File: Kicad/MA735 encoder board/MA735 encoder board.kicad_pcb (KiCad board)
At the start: 2 copper layers, 10.4 x 9.5 mm, 5 parts, among them J2 JST SH SM06B, U1 MA735GGU-Z

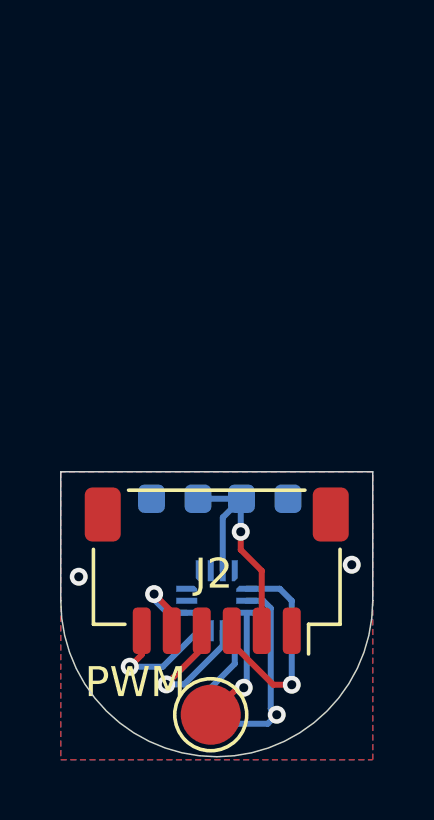
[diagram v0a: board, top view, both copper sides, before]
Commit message: Start redesign of encoder board for flex circuit
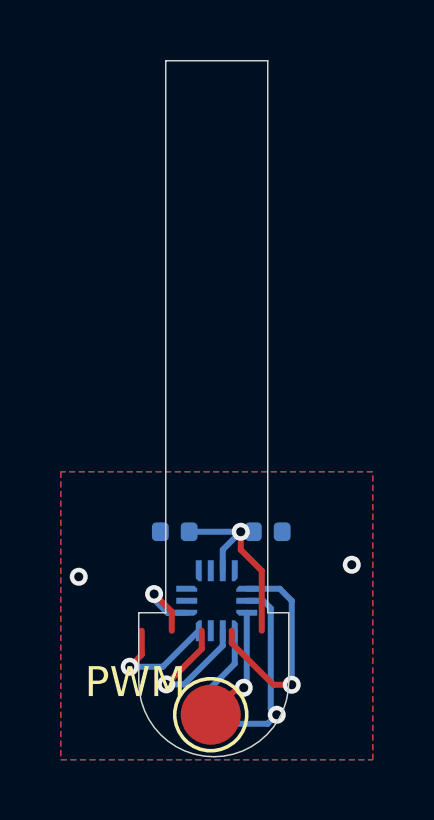
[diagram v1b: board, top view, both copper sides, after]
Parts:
- removed J2: JST SH SM06B, Connector_JST:JST_SH_SM06B-SRSS-TB_1x06-1MP_P1.00mm_Horizontal
- C1, C2: footprint Capacitor_SMD:C_0603_1608Metric -> Capacitor_SMD:C_0402_1005Metric
- moved C1 1.10 mm to (154.1, 84.5)
- moved C2 1.10 mm to (151.0, 84.5)
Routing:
- net +3V3: track 8.77 -> 7.28 mm
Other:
- board size 10.4 x 9.5 mm -> 5 x 23.2 mm

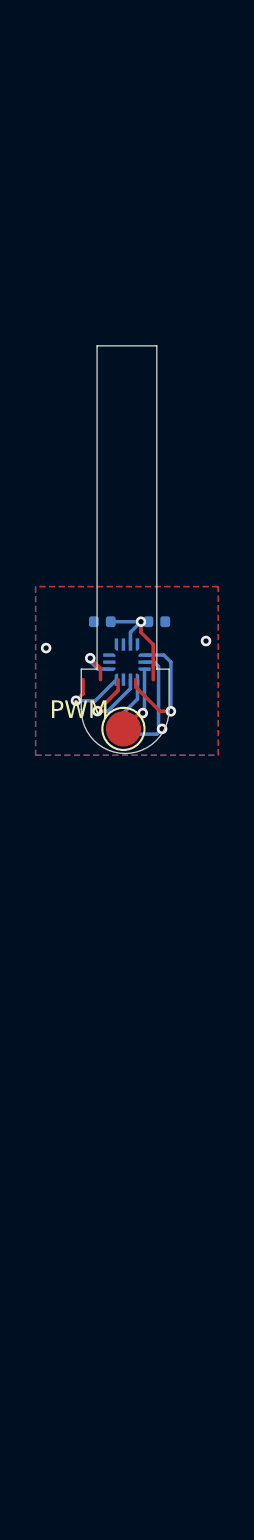
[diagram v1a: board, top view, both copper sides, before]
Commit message: Partial layout complete
I currently have the board sized at 4.5mm with a really long cable. This is probably WAY to small, I can barely fit the 0402 capacitors.
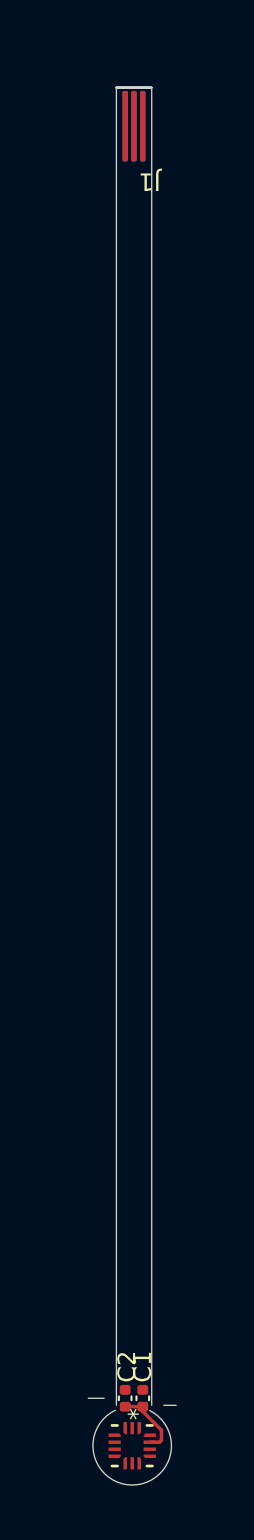
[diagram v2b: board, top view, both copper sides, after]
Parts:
- removed TP1: TestPoint, TestPoint:TestPoint_Pad_D2.0mm
- added J1: FPC top, custom_testpoints:3pin_fpc, F.Cu at (152.8, 56.3)
- added J2: FPC bottom, custom_testpoints:3pin_fpc, B.Cu at (152.8, 56.3)
- C1, C2, U1: moved to F.Cu
- moved U1 44.6 mm to (152.7, 131.4), turned to -90 degrees
- moved C2 44.2 mm to (152.3, 128.7), turned to 90 degrees
- moved C1 44.2 mm to (153.3, 128.7), turned to 90 degrees
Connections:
- U1 pad 3: /PWM -> unconnected-(U1-PWM-Pad3)
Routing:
- net GND: track 10.3 -> 0.00 mm, vias 3 -> 0
- net /SCK: track 7.45 -> 0.00 mm, vias 1 -> 0
- net /MISO: track 5.19 -> 0.00 mm, vias 1 -> 0
- net /CS: track 4.16 -> 0.00 mm, vias 1 -> 0
- net /PWM: track 4.01 -> 0.00 mm, vias 1 -> 0
- net +3V3: track 7.28 -> 4.06 mm, vias 1 -> 0
- net /MOSI: track 2.93 -> 0.00 mm, vias 1 -> 0
- removed copper zone on B.Cu, net GND
- removed copper zone on F.Cu, net GND
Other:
- board size 5 x 23.2 mm -> 5 x 79.5 mm
- board text removed: "PWM"

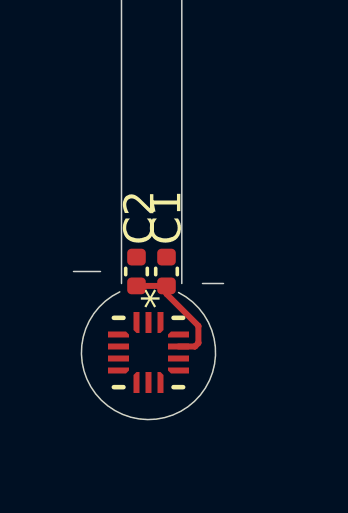
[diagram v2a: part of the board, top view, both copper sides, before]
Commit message: Mostly completed routing
I have reached the minimum obtainable space, 5.6mm diameter. I don't think is not worth it to try shrinking it smaller
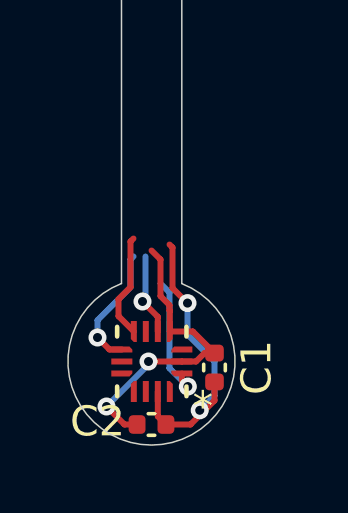
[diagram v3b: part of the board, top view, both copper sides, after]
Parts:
- moved C2 5.12 mm to (152.8, 133.8), turned to 180 degrees
- moved C1 3.58 mm to (154.9, 131.9)
- moved U1 0.32 mm to (152.8, 131.7), turned to 180 degrees
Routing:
- net GND: track 0.00 -> 10.4 mm, vias 0 -> 2
- net +3V3: track 4.06 -> 10.1 mm, vias 0 -> 2
- net /SCK: track 0.00 -> 4.33 mm, vias 0 -> 1
- net /MOSI: track 0.00 -> 4.17 mm, vias 0 -> 1
- net /CS: track 0.00 -> 3.52 mm
- net /MISO: track 0.00 -> 2.75 mm, vias 0 -> 1
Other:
- board size 5 x 79.5 mm -> 5.6 x 80.4 mm

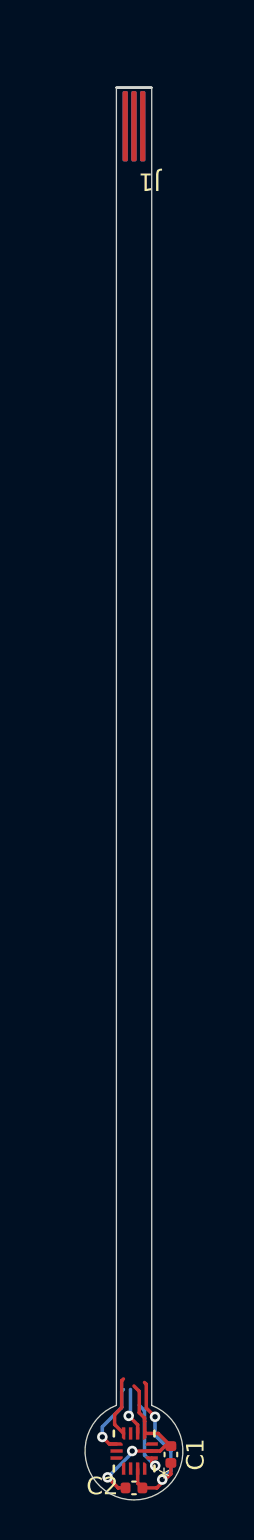
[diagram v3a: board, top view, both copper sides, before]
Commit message: Started work on FPC edge connector
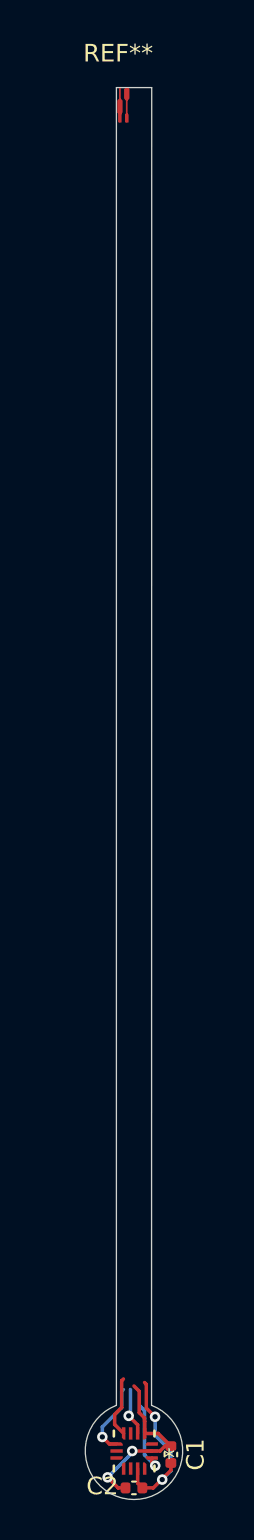
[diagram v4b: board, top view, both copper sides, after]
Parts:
- removed J1: FPC top, custom_testpoints:3pin_fpc
- removed J2: FPC bottom, custom_testpoints:3pin_fpc
- added REF**: 7pin_fpc_contact_0.3mmptich, custom_testpoints:7pin_fpc_contact_0.3mmptich, F.Cu at (152.8, 55.3)
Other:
- board size 5.6 x 80.4 mm -> 5.5 x 80.4 mm
- board text added: "Minimum solder mask is 0.5mm. I have to remove more around the edge connector and the encode"

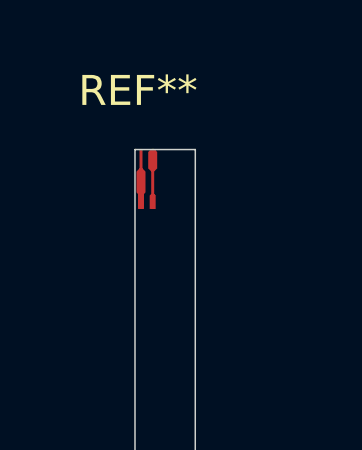
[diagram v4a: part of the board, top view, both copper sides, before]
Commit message: Finished 7pin fpc contacts
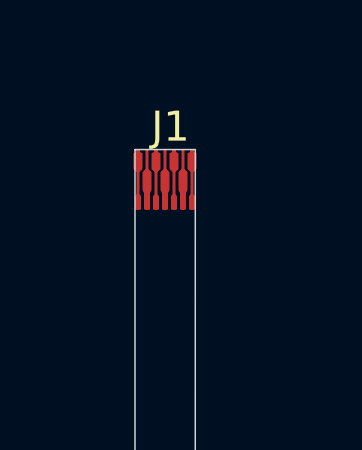
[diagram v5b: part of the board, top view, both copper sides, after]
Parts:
- removed REF**: 7pin_fpc_contact_0.3mmptich, custom_testpoints:7pin_fpc_contact_0.3mmptich
- added J1: FPC contacts 0.3mm, custom_testpoints:7pin_fpc_contact_0.3mmptich, F.Cu at (152.8, 55.2)
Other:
- board text added: "Fits connector: AYF330735 from panasonic"
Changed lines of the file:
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@@
 	(footprint "custom_testpoints:7pin_fpc_contact_0.3mmptich"
 		(layer "F.Cu")
-		(at 152.8 55.3)
-		(property "Reference" "REF**"
-			(at -0.9 -3.15 0)
+		(at 152.8 55.2)
+		(property "Reference" "J1"
+			(at 0.18 -1.86 0)
 			(unlocked yes)
 			(layer "F.SilkS")
@@
 			)
 		)
-		(property "Value" "7pin_fpc_contact_0.3mmptich"
-			(at 4.74 -0.37 0)
+		(property "Value" "FPC contacts 0.3mm"
+			(at 1 0.8 0)
 			(unlocked yes)
 			(layer "F.Fab")
@@
 		)
 		(property "Footprint" "custom_testpoints:7pin_fpc_contact_0.3mmptich"
-			(at 0 0 0)
+			(at -0.1 0.12 0)
 			(unlocked yes)
 			(layer "F.Fab")
@@
 		)
 		(property "Datasheet" ""
-			(at 0 0 0)
+			(at -0.1 0.12 0)
 			(unlocked yes)
 			(layer "F.Fab")
@@
 			)
 		)
-		(property "Description" ""
-			(at 0 0 0)
+		(property "Description" "Generic connector, single row, 01x07, script generated"
+			(at -0.1 0.12 0)
 			(unlocked yes)
 			(layer "F.Fab")
@@
 			)
 		)
+		(property ki_fp_filters "Connector*:*_1x??_*")
+		(sheetname "Root")
+		(sheetfile "MA735 encoder board.kicad_sch")
 		(attr smd)
+		(fp_rect
+			(start -1.2 -1.1)
+			(end 1.2 1.9)
+			(stroke
+				(width 0.05)
+				(type default)
+			)
+			(fill none)
+			(layer "Dwgs.User")
+		)
+		(fp_text user "Stiffener box"
+			(at -2.65 2.54 0)
+			(unlocked yes)
+			(layer "Dwgs.User" knockout)
+			(effects
+				(font
+					(size 0.5 0.5)
+					(thickness 0.1)
+					(bold yes)
+				)
+				(justify left bottom)
+			)
+		)
 		(fp_text user "${REFERENCE}"
-			(at 6.41 -2.22 0)
+			(at 0.33 -0.35 0)
 			(unlocked yes)
 			(layer "F.Fab")
@@
 		)
 		(pad "1" connect custom
-			(at -0.8 -0.22)
-			(size 0.1 2)
-			(layers "F.Cu" "F.Mask")
-			(options
-				(clearance outline)
-				(anchor rect)
-			)
-			(primitives
+			(at -0.9 -0.1)
+			(size 0.1 2)
+			(layers "F.Cu" "F.Mask")
+			(net 3 "/MOSI")
+			(pinfunction "Pin_1")
+			(pintype "passive")
+			(options
+				(clearance outline)
+				(anchor rect)
+			)
+			(primitives
+				(gr_poly
+					(pts
+						(xy -0.1 0.55) (xy -0.05 0.5) (xy 0.05 0.5) (xy 0.1 0.55) (xy 0.1 1) (xy -0.1 1)
+					)
+					(width 0)
+					(fill yes)
+				)
+				(gr_poly
+					(pts
+						(xy -0.15 -0.88) (xy -0.12 -0.89) (xy -0.08 -0.91) (xy -0.06 -0.94) (xy -0.05 -0.97) (xy -0.05 -1)
+						(xy 0.05 -1) (xy 0.05 -0.97) (xy 0.06 -0.94) (xy 0.08 -0.91) (xy 0.12 -0.89) (xy 0.15 -0.88) (xy 0.15 -0.35)
+						(xy 0.05 -0.25) (xy -0.05 -0.25) (xy -0.15 -0.35)
+					)
+					(width 0)
+					(fill yes)
+				)
+			)
+		)
+		(pad "2" connect custom
+			(at -0.6 -0.1)
+			(size 0.1 2)
+			(layers "F.Cu" "F.Mask")
+			(net 1 "GND")
+			(pinfunction "Pin_2")
+			(pintype "passive")
+			(options
+				(clearance outline)
+				(anchor rect)
+			)
+			(primitives
+				(gr_poly
+					(pts
+						(xy -0.15 -0.25) (xy -0.05 -0.35) (xy 0.05 -0.35) (xy 0.15 -0.25) (xy 0.15 0.35) (xy 0.1 0.45)
+						(xy -0.1 0.45) (xy -0.15 0.35)
+					)
+					(width 0)
+					(fill yes)
+				)
 				(gr_poly
 					(pts
@@
 					(fill yes)
 				)
-				(gr_poly
-					(pts
-						(xy -0.15 -0.25) (xy -0.05 -0.35) (xy 0.05 -0.35) (xy 0.15 -0.25) (xy 0.15 0.45) (xy 0.05 0.55)
-						(xy -0.05 0.55) (xy -0.15 0.45)
-					)
-					(width 0)
-					(fill yes)
-				)
-			)
-		)
-		(pad "2" connect custom
-			(at -0.41 -0.22)
-			(size 0.1 2)
-			(layers "F.Cu" "F.Mask")
-			(options
-				(clearance outline)
-				(anchor rect)
-			)
-			(primitives
-				(gr_poly
-					(pts
-						(xy -0.15 -0.9) (xy -0.05 -1) (xy 0.05 -1) (xy 0.15 -0.9) (xy 0.15 -0.35) (xy 0.05 -0.25) (xy -0.05 -0.25)
-						(xy -0.15 -0.35)
-					)
-					(width 0)
-					(fill yes)
-				)
+			)
+		)
+		(pad "3" connect custom
+			(at -0.3 -0.1)
+			(size 0.1 2)
+			(layers "F.Cu" "F.Mask")
+			(net 4 "/MISO")
+			(pinfunction "Pin_3")
+			(pintype "passive")
+			(options
+				(clearance outline)
+				(anchor rect)
+			)
+			(primitives
 				(gr_poly
 					(pts
 						(xy -0.1 0.55) (xy -0.05 0.5) (xy 0.05 0.5) (xy 0.1 0.55) (xy 0.1 1) (xy -0.1 1)
+					)
+					(width 0)
+					(fill yes)
+				)
+				(gr_poly
+					(pts
+						(xy -0.15 -0.88) (xy -0.12 -0.89) (xy -0.08 -0.91) (xy -0.06 -0.94) (xy -0.05 -0.97) (xy -0.05 -1)
+						(xy 0.05 -1) (xy 0.05 -0.97) (xy 0.06 -0.94) (xy 0.08 -0.91) (xy 0.12 -0.89) (xy 0.15 -0.88) (xy 0.15 -0.35)
+						(xy 0.05 -0.25) (xy -0.05 -0.25) (xy -0.15 -0.35)
+					)
+					(width 0)
+					(fill yes)
+				)
+			)
+		)
+		(pad "4" connect custom
+			(at 0 -0.1)
+			(size 0.1 2)
+			(layers "F.Cu" "F.Mask")
+			(net 1 "GND")
+			(pinfunction "Pin_4")
+			(pintype "passive")
+			(options
+				(clearance outline)
+				(anchor rect)
+			)
+			(primitives
+				(gr_poly
+					(pts
+						(xy -0.15 -0.25) (xy -0.05 -0.35) (xy 0.05 -0.35) (xy 0.15 -0.25) (xy 0.15 0.35) (xy 0.1 0.45)
+						(xy -0.1 0.45) (xy -0.15 0.35)
+					)
+					(width 0)
+					(fill yes)
+				)
+				(gr_poly
+					(pts
+						(xy -0.1 0.45) (xy 0.1 0.45) (xy 0.1 1) (xy -0.1 1)
+					)
+					(width 0)
+					(fill yes)
+				)
+			)
+		)
+		(pad "5" connect custom
+			(at 0.3 -0.1)
+			(size 0.1 2)
+			(layers "F.Cu" "F.Mask")
+			(net 6 "/SCK")
+			(pinfunction "Pin_5")
+			(pintype "passive")
+			(options
+				(clearance outline)
+				(anchor rect)
+			)
+			(primitives
+				(gr_poly
+					(pts
+						(xy -0.1 0.55) (xy -0.05 0.5) (xy 0.05 0.5) (xy 0.1 0.55) (xy 0.1 1) (xy -0.1 1)
+					)
+					(width 0)
+					(fill yes)
+				)
+				(gr_poly
+					(pts
+						(xy -0.15 -0.88) (xy -0.12 -0.89) (xy -0.08 -0.91) (xy -0.06 -0.94) (xy -0.05 -0.97) (xy -0.05 -1)
+						(xy 0.05 -1) (xy 0.05 -0.97) (xy 0.06 -0.94) (xy 0.08 -0.91) (xy 0.12 -0.89) (xy 0.15 -0.88) (xy 0.15 -0.35)
+						(xy 0.05 -0.25) (xy -0.05 -0.25) (xy -0.15 -0.35)
+					)
+					(width 0)
+					(fill yes)
+				)
+			)
+		)
+		(pad "6" connect custom
+			(at 0.6 -0.1)
+			(size 0.1 2)
+			(layers "F.Cu" "F.Mask")
+			(net 2 "+3V3")
+			(pinfunction "Pin_6")
+			(pintype "passive")
+			(options
+				(clearance outline)
+				(anchor rect)
+			)
+			(primitives
+				(gr_poly
+					(pts
+						(xy -0.15 -0.25) (xy -0.05 -0.35) (xy 0.05 -0.35) (xy 0.15 -0.25) (xy 0.15 0.35) (xy 0.1 0.45)
+						(xy -0.1 0.45) (xy -0.15 0.35)
+					)
+					(width 0)
+					(fill yes)
+				)
+				(gr_poly
+					(pts
+						(xy -0.1 0.45) (xy 0.1 0.45) (xy 0.1 1) (xy -0.1 1)
+					)
+					(width 0)
+					(fill yes)
+				)
+			)
+		)
+		(pad "7" connect custom
+			(at 0.9 -0.1)
+			(size 0.1 2)
+			(layers "F.Cu" "F.Mask")
+			(net 5 "/CS")
+			(pinfunction "Pin_7")
+			(pintype "passive")
+			(options
+				(clearance outline)
+				(anchor rect)
+			)
+			(primitives
+				(gr_poly
+					(pts
+						(xy -0.1 0.55) (xy -0.05 0.5) (xy 0.05 0.5) (xy 0.1 0.55) (xy 0.1 1) (xy -0.1 1)
+					)
+					(width 0)
+					(fill yes)
+				)
+				(gr_poly
+					(pts
+						(xy -0.15 -0.88) (xy -0.12 -0.89) (xy -0.08 -0.91) (xy -0.06 -0.94) (xy -0.05 -0.97) (xy -0.05 -1)
+						(xy 0.05 -1) (xy 0.05 -0.97) (xy 0.06 -0.94) (xy 0.08 -0.91) (xy 0.12 -0.89) (xy 0.15 -0.88) (xy 0.15 -0.35)
+						(xy 0.05 -0.25) (xy -0.05 -0.25) (xy -0.15 -0.35)
 					)
 					(width 0)
@@
 		(layer "Edge.Cuts")
 	)
+	(gr_text "Fits connector: AYF330735 from panasonic"
+		(at 144.8 48.3 0)
+		(layer "Cmts.User")
+		(effects
+			(font
+				(size 1 1)
+				(thickness 0.15)
+			)
+			(justify left bottom)
+		)
+	)
 	(gr_text "Minimum solder mask is 0.5mm. I have to remove more around the edge connector and the encode"
 		(at 144 139.6 0)
@@
 		(layer "Cmts.User")
 		(pts
-			(xy 151.8 54.1) (xy 153.81 54.1)
+			(xy 151.6 54.1) (xy 154 54.1)
 		)
 		(height -1.9)
-		(gr_text "2.0100 mm"
-			(at 152.805 51.575 0)
+		(gr_text "2.4000 mm"
+			(at 152.8 51.575 0)
 			(layer "Cmts.User")
 			(effects

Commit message: Wiring
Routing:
- net GND: track 10.4 -> 18.5 mm
- net /SCK: track 4.33 -> 6.61 mm, vias 1 -> 2
- net /MOSI: track 4.17 -> 5.71 mm, vias 1 -> 0
- net /MISO: track 2.75 -> 3.13 mm, vias 1 -> 0
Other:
- board size 5.5 x 80.4 mm -> 5.7 x 80.4 mm

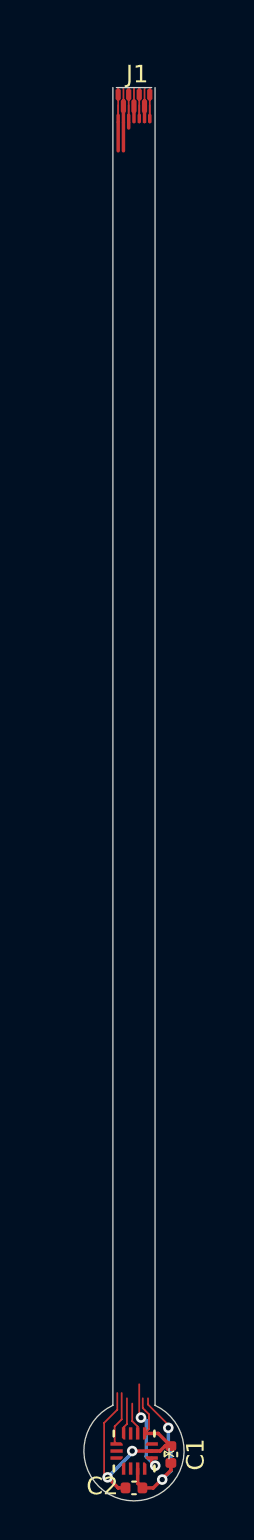
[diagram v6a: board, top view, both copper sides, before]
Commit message: Changed everything to 0.2mm traces and 0.3mm vias for cost
Its a tight fit but everything works out okay. Note that the trace minimum gap is half of the typical, its at 0.1mm. Most board manufactures should be able to handle this, but it may still add an additional cost
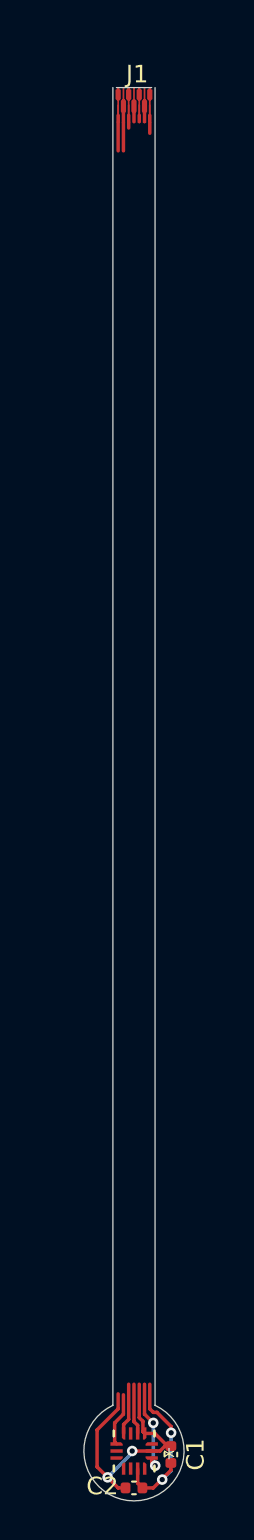
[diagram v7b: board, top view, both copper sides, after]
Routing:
- net /CS: track 3.08 -> 4.52 mm
- net /MISO: track 3.13 -> 4.19 mm
- net GND: track 18.5 -> 19.5 mm
- net +3V3: track 10.0 -> 10.9 mm
